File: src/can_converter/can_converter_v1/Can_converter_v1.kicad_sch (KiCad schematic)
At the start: 19 parts, among them P1 CONN_01X02, T101 Tab, T102 Tab, T103 Tab, T104 Tab, X1 629722000214_pasteInHole

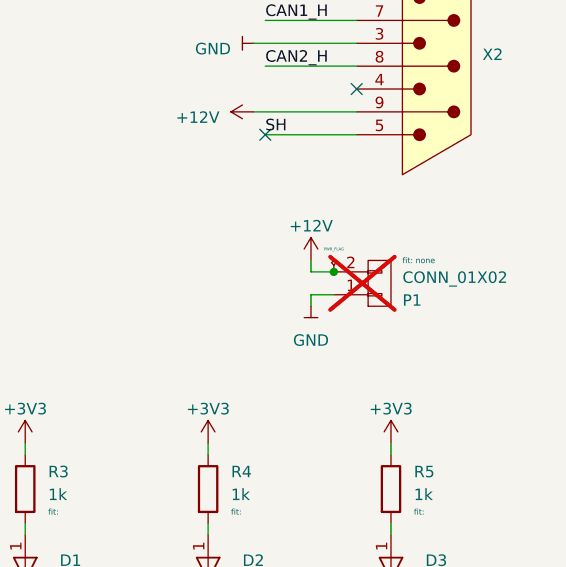
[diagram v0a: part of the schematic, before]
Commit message: Replace regulator and tranceiver
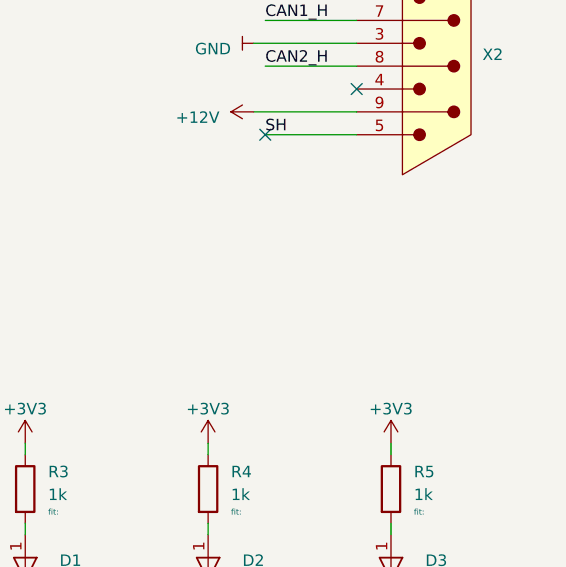
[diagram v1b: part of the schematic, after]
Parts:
- removed P1: CONN_01X02, Connector_generic:Header_1x2_Pitch2.54mm, symbol generic-connectors:CONN_01X02
